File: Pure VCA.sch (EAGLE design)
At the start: 33 parts, among them U1 DUAL_OPAMP, U2 THAT_2181_SMD

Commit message: VCA 2.2
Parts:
- removed U1: DUAL_OPAMP, INSTRUO:DUAL_OPAMP
- removed U2: THAT_2181_SMD, INSTRUO:THAT_2181_SMD
- added IC1: TL072, GMSN:OPAMP_DUALD
- added IC2: THAT2181, GMSN:VCA_THAT2181
- BUSS: value M02PTH -> HEADER1X2PTH; device SparkFun-Connectors:M02PTH -> GMSN:HEADER1X2PTH
- C1, C3: device rcl:C-USC0805K -> GMSN:CAPACITOR-USC0805
- C2, C4, C5: value 10u -> 10uF; device rcl:CPOL-US153CLV-0505 -> GMSN:CAPACITOR_POL-US153CLV-0505
- C6, C7, C8, C9: value 0.1u -> 100nF; device rcl:C-USC0805K -> GMSN:CAPACITOR-USC0805
- CV_IN, SIG_IN, SIG_OUT: value S_JACK -> PJ301M-12; device INSTRUO:S_JACK -> GMSN:SOCKET_MONO_3.5MMPJ301M-12
- CV_LEVEL, OFFSET: value 50K -> B100k; device INSTRUO:Q-POT -> GMSN:RESISTOR_VARIABLE9MM_POT
- D1, D2: value (none) -> STTH102A; device adafruit:DIODESMA -> GMSN:DIODESMA
- PWR: value M05X2SHD -> HEADER2X5SHD; device SparkFun-Connectors:M05X2SHD -> GMSN:HEADER2X5SHD
- R1: value 47K -> 20k; device rcl:R-US_R0805 -> GMSN:RESISTOR_USR0805
- R10: value 220K* -> 130k; device rcl:R-US_R0805 -> GMSN:RESISTOR_USR0805
- R11, R5: device rcl:R-US_R0805 -> GMSN:RESISTOR_USR0805
- R12: value 19K1 -> 19k1; device rcl:R-US_R0805 -> GMSN:RESISTOR_USR0805
- R2: value 47K -> 2k2; device rcl:R-US_R0805 -> GMSN:RESISTOR_USR0805
- R3: value 47K -> 75k; device rcl:R-US_R0805 -> GMSN:RESISTOR_USR0805
- R4: value 13K -> 100R; device rcl:R-US_R0805 -> GMSN:RESISTOR_USR0805
- R6, R8: value 20K -> 20k; device rcl:R-US_R0805 -> GMSN:RESISTOR_USR0805
- R7: value 4K12 -> 4k12; device rcl:R-US_R0805 -> GMSN:RESISTOR_USR0805
- R9: value 1K -> 1k; device rcl:R-US_R0805 -> GMSN:RESISTOR_USR0805
- TR1: value 50K -> 50k; device INSTRUO:TRIM_3269W -> GMSN:RESISTOR_VARIABLETRIMMER_TH
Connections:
- removed net N$10: C2.-, R6.2
- net +12V: now also IC1P.V+, IC2.V+; no longer U1G$3.+12V, U2.V+
- net -12V: now also IC1P.V-; no longer U1G$4.-12V
- net GND: now also CV_IN.SLEEVE, IC1B.+IN, IC2.EC+, IC2.GND, SIG_IN.SLEEVE, SIG_IN.SWITCH, SIG_OUT.SLEEVE; no longer CV_IN.GND, SIG_IN.GND, SIG_IN.NORM, SIG_OUT.GND, U1G$2.+IN, U2.EC+, U2.GND
- net N$11: now also C2.-, R6.2
- net N$12: now also SIG_OUT.SWITCH; no longer SIG_OUT.NORM
- net N$13: now also IC2.V-; no longer U2.V-
- net N$14: now also IC1A.+IN; no longer U1G$1.+IN
- net N$15: now also IC1B.-IN, IC2.OUT; no longer U1G$2.-IN, U2.OUT
- net N$16: now also IC1B.OUT; no longer U1G$2.OUT
- net N$17: now also IC2.SYM; no longer U2.SYM
- net N$2: now also IC1A.-IN; no longer U1G$1.-IN
- net N$5: now also IC1A.OUT, IC2.EC-; no longer U1G$1.OUT, U2.EC-
- net N$9: now also IC2.-IN; no longer U2.-IN

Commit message: VCA 2.3
VCA Updated to V2.3 14/4/21

Library updated to include 3D models.
Traces rerouted.
Weird shorted cap removed. WTF?
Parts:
- removed BUSS: HEADER1X2PTH, GMSN:HEADER1X2PTH
- removed C2: 10uF, GMSN:CAPACITOR_POL-US153CLV-0505
- CV_LEVEL: device GMSN:RESISTOR_VARIABLE9MM_POT -> GMSN:RESISTOR_VARIABLEPOT_9MM_GREEN_KNOB
- OFFSET: device GMSN:RESISTOR_VARIABLE9MM_POT -> GMSN:RESISTOR_VARIABLEPOT_9MM_BLUE_KNOB
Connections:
- removed net N$12: BUSS.1, SIG_OUT.SWITCH
- net GND: now also CV_IN.SWITCH; no longer BUSS.2
- net N$11: no longer C2.+, C2.-

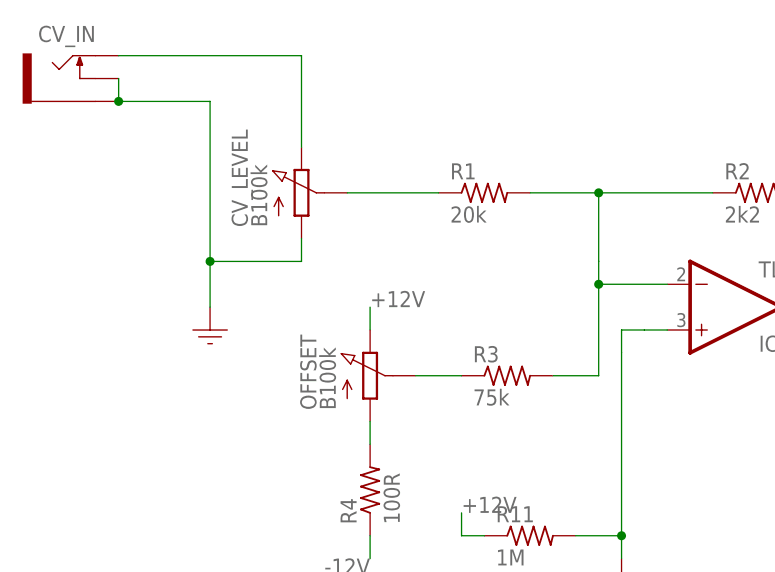
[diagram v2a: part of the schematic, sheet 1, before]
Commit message: VCA 2.31
VCA Updated to V2.31 14/4/21

Library updated to include 3D models.
Traces rerouted.
Weird shorted cap removed. WTF?
Values tweaked for better CV response.
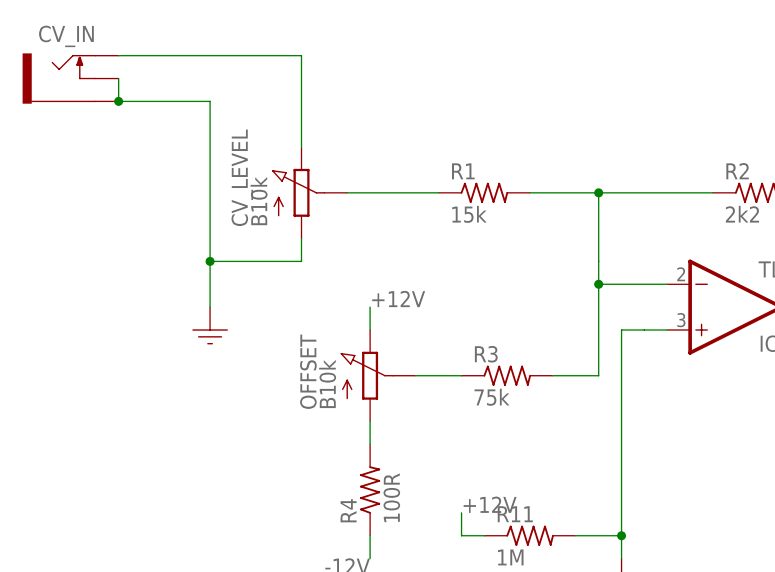
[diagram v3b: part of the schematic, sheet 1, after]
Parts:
- CV_LEVEL, OFFSET: value B100k -> B10k
- R1: value 20k -> 15k
